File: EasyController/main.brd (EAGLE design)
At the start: 91 x 76 mm, 53 parts, among them IC2 L6387EDIP8, IC3 L6387EDIP8, IC4 L6387EDIP8, J3 FUSE

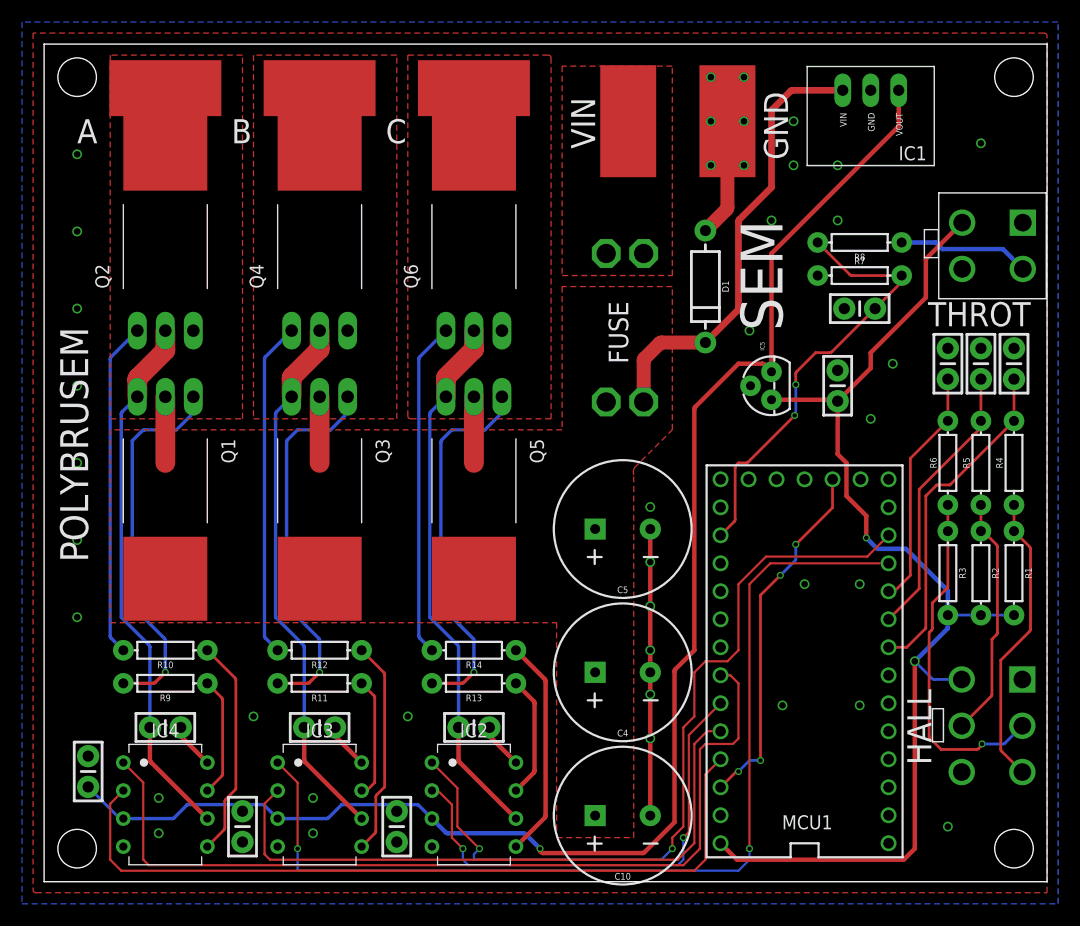
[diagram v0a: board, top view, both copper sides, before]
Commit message: CAN transceiver
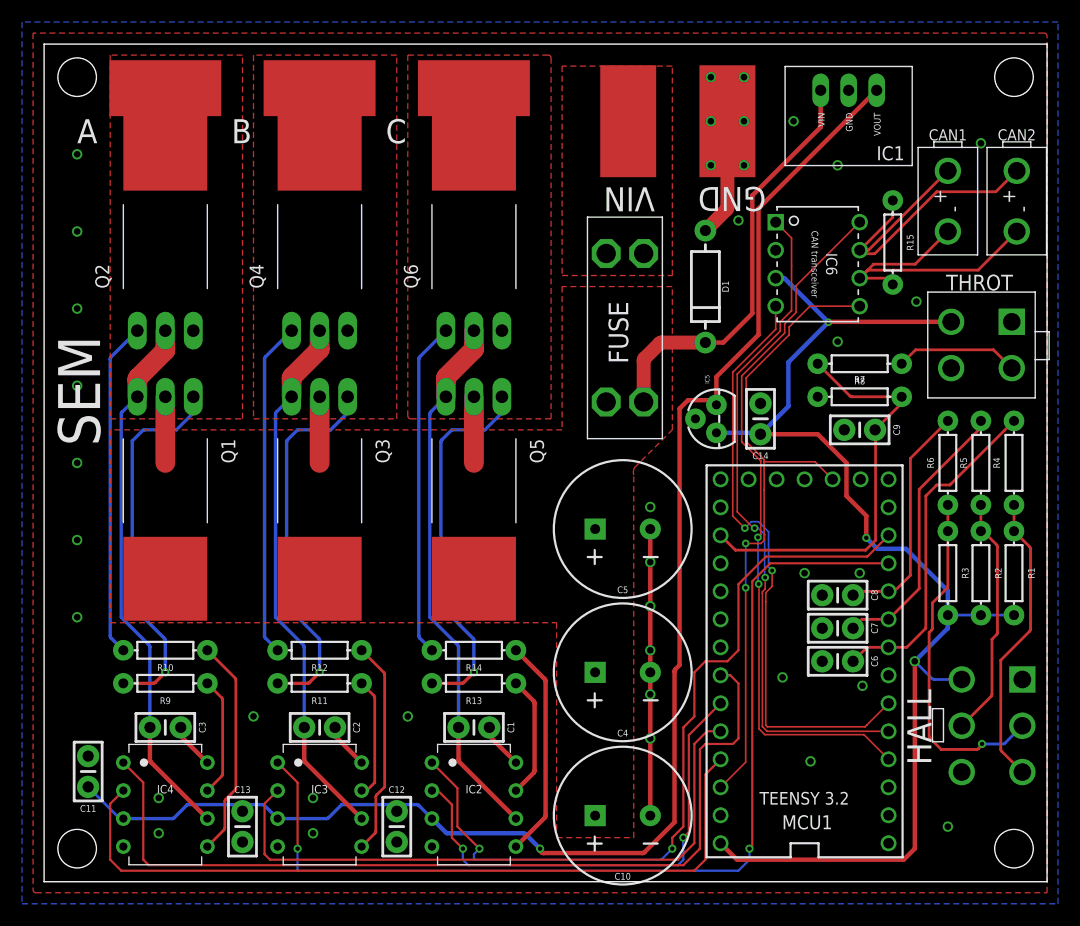
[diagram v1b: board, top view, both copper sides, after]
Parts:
- added CAN1, CAN2: HEADER2, Custom_old:2PINVALULOK
- added IC6: MCP2562-E/P, Custom_new:PDIP8_300MC
- added R15: 120, SparkFun-Resistors:AXIAL-0.3
- added U$3, U$9: (no value), Custom_old:DEV
- moved C6 31.4 mm to (72.0, 20.0), turned to 180 degrees
- moved C7 27.3 mm to (72.0, 23.0), turned to 180 degrees
- moved C8 23.3 mm to (72.0, 26.0), turned to 180 degrees
- moved C9 11.0 mm to (74.0, 41.0)
- moved R7 11.0 mm to (74.0, 44.0)
- moved R8 11.0 mm to (74.0, 47.0)
- moved U$1 9.06 mm to (82.3, 50.8)
- moved C14 7.62 mm to (65.0, 42.0)
- moved IC5 5.83 mm to (61.0, 42.0)
- moved IC1 2.00 mm to (73.0, 68.0)
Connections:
- new net CANH: CAN1.1, CAN2.1, IC6.7, R15.P$1
- new net CANL: CAN1.2, CAN2.2, IC6.6, R15.P$2
- new net DI: IC6.1, MCU1.3
- new net EN_CAN: IC6.8, MCU1.2
- new net RO: IC6.4, MCU1.4
- net 3.3V: now also IC6.5
- net 5V: now also IC6.3
- net GND: now also IC6.2
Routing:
- net EN_CAN: track 0.00 -> 64.2 mm, vias 0 -> 2
- net DI: track 0.00 -> 61.4 mm, vias 0 -> 2
- net RO: track 0.00 -> 55.0 mm, vias 0 -> 2
- net CANH: track 0.00 -> 34.2 mm
- net CANL: track 0.00 -> 28.5 mm
- net 3.3V: track 33.0 -> 61.3 mm, vias 4 -> 2
- net 5V: track 104.0 -> 114.4 mm, vias 2 -> 3
- net THROTTLE: track 40.5 -> 37.9 mm, vias 2 -> 0
- net V_RAW: track 58.8 -> 56.2 mm
- net VDD: track 137.7 -> 136.3 mm
- net N$7: track 12.0 -> 11.2 mm
- net GND: vias 39 -> 37
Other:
- board text added: "BLDC Controller 1.2 Designed by PLG, Feb 2019 DEV, Shell Eco-Marathon"
- board text added: "CANH"
- board text added: "CANL"
- board text added: "TEENSY 3.2"
- board text removed: "BLDC Controller 1.1 Designed by PLG, Feb 2019 POLYBRUSEM, Shell Eco-Marathon"
- board text removed: "POLYBRUSEM"
